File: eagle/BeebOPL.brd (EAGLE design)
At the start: 100 x 80 mm, 34 parts, among them IC1 LM324N, IC2 YM3014B, IC5 74LS02N, IC6 YM3812, IC7 74LS04N, IC9 74HCT688N, J1 1 MHz Bus, J2 Feed-through, J3 3.5mm Jack, J4 5V DC

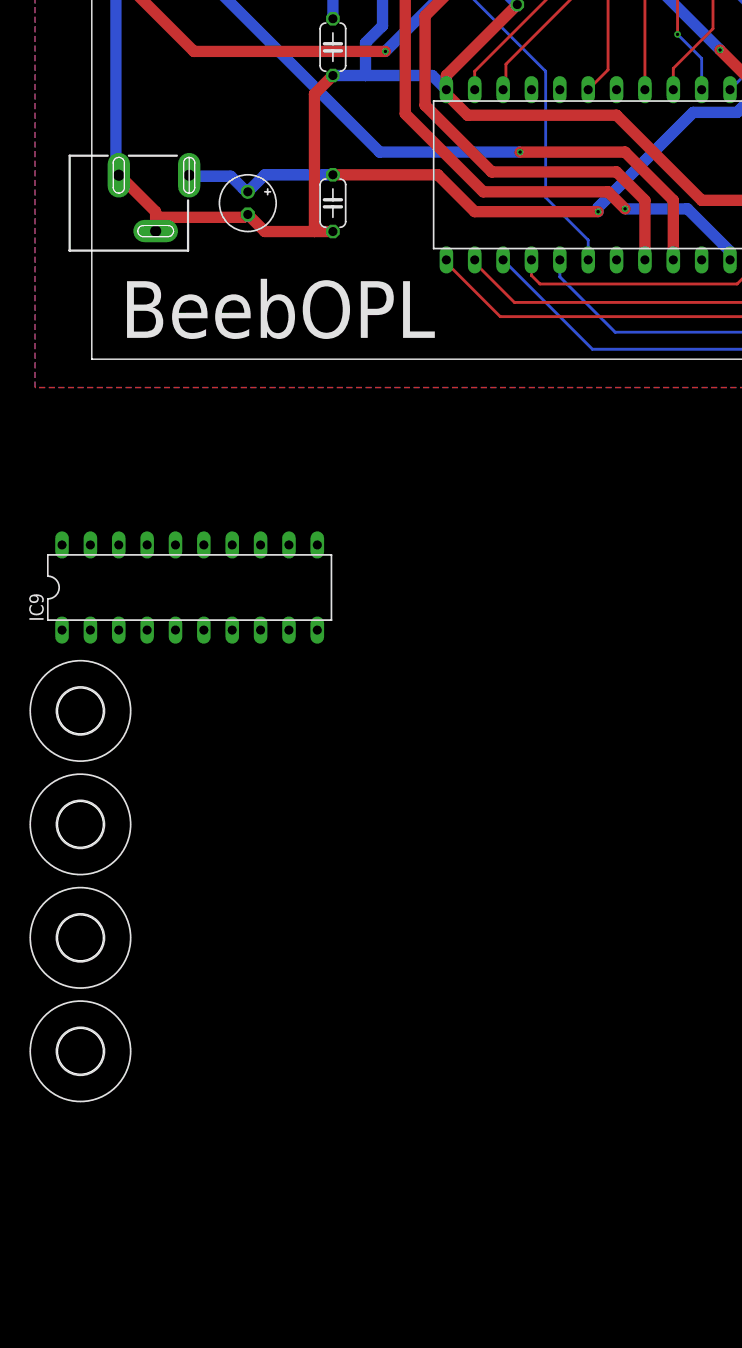
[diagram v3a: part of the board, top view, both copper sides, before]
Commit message: Added resistor networks
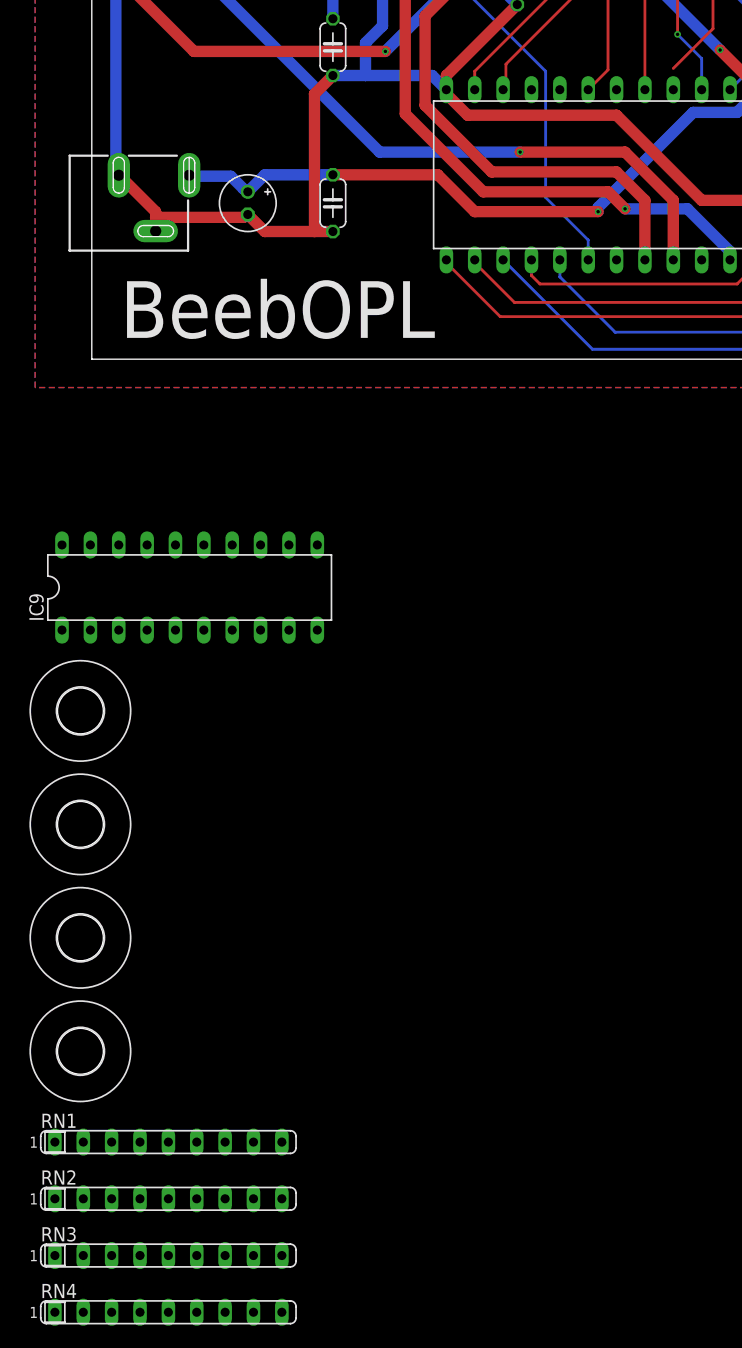
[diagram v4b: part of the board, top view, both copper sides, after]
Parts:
- added RN1, RN2, RN3, RN4: 2K2, resistor-sil:SIL9
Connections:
- net A0: now also RN3.2, RN4.2
- net A1: now also RN3.3, RN4.3
- net A2: now also RN3.4, RN4.4
- net A3: now also RN3.5, RN4.5
- net A4: now also RN3.6, RN4.6
- net A5: now also RN3.7, RN4.7
- net A6: now also RN3.8, RN4.8
- net A7: now also RN3.9, RN4.9
- net D0: now also RN1.2, RN2.2
- net D1: now also RN1.3, RN2.3
- net D2: now also RN1.4, RN2.4
- net D3: now also RN1.5, RN2.5
- net D4: now also RN1.6, RN2.6
- net D5: now also RN1.7, RN2.7
- net D6: now also RN1.8, RN2.8
- net D7: now also RN1.9, RN2.9
- net GND: now also RN2.1, RN4.1
- net VCC: now also RN1.1, RN3.1
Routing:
- net A0: track 77.6 -> 75.7 mm

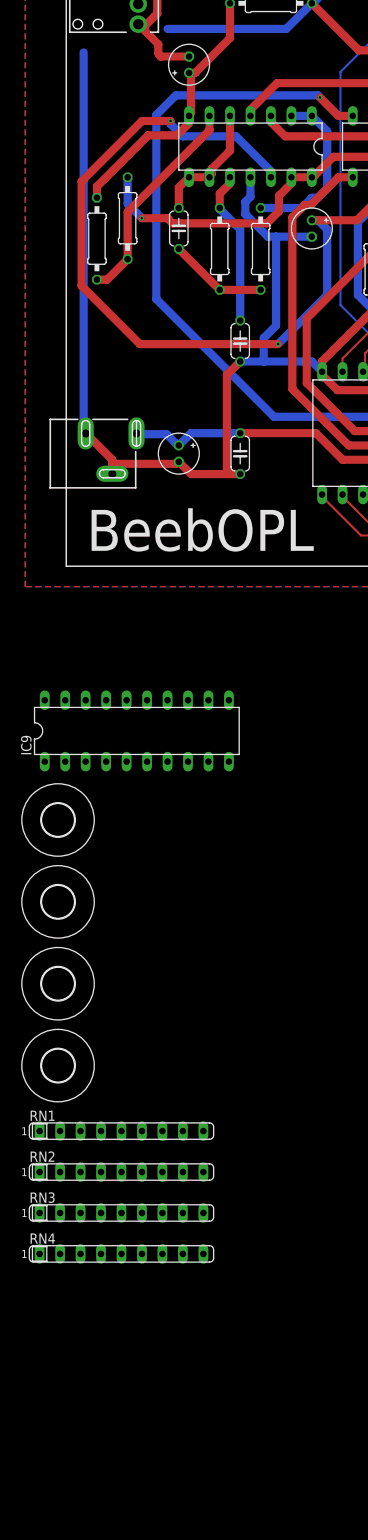
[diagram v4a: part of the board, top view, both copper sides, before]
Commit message: Added optional power regualtor
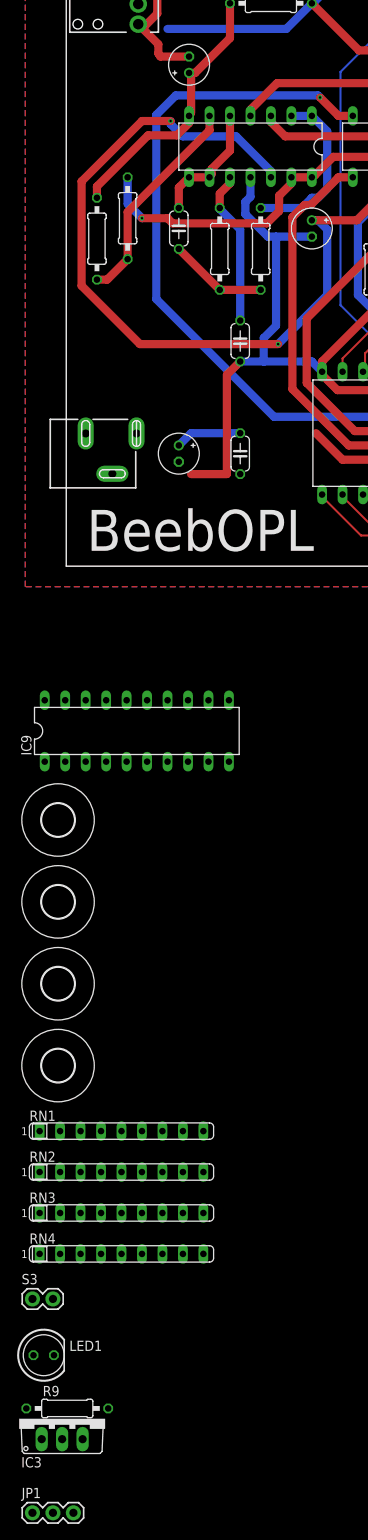
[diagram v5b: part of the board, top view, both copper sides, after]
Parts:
- added IC3: 7805TV, linear:TO220V
- added JP1: JUMPER-3PTH, SparkFun-Retired:1X03
- added LED1: (no value), led:LED5MM
- added R9: 470R, resistor:0207/10
- added S3: LED, SparkFun-Retired:1X02
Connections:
- new net N$25: LED1.A, R9.1, S3.2
- new net N$27: IC3.1, JP1.3
- new net N$28: C6.-, C7.2
- new net N$29: C6.+, C7.1
- net GND: now also IC3.2, LED1.K, S3.1; no longer C6.-, C7.2, J4.GND@1
- net VCC: now also IC3.3, JP1.1, JP1.2, R9.2; no longer C6.+, C7.1
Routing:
- net GND: track 408.9 -> 343.0 mm
- net VCC: track 186.5 -> 163.0 mm
- net N$29: track 0.00 -> 8.25 mm
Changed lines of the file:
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@@
 <attribute name="MF" value="" x="6.858" y="-85.344" size="1.778" layer="27" display="off"/>
 </element>
+<element name="S3" library="SparkFun-Retired" package="1X02" value="LED" x="-4.191" y="-90.932"/>
+<element name="LED1" library="led" package="LED5MM" value="" x="-2.794" y="-97.917"/>
+<element name="R9" library="resistor" package="0207/10" value="470R" x="0.127" y="-104.521"/>
+<element name="IC3" library="linear" package="TO220V" value="7805TV" x="-0.508" y="-105.791"/>
+<element name="JP1" library="SparkFun-Retired" package="1X03" value="JUMPER-3PTH" x="-4.191" y="-117.475"/>
 </elements>
 <signals>
@@
 <contactref element="C4" pad="2"/>
 <contactref element="IC5" pad="7"/>
-<contactref element="J4" pad="GND@1"/>
-<contactref element="J4" pad="GND@2"/>
-<contactref element="C6" pad="-"/>
-<contactref element="C7" pad="2"/>
 <contactref element="IC6" pad="GND"/>
 <contactref element="C8" pad="2"/>
@@
 <wire x1="74.1045" y1="20.6375" x2="64.389" y2="30.353" width="1.016" layer="1"/>
 <wire x1="15.494" y1="11.43" x2="19.939" y2="11.43" width="1.016" layer="1"/>
-<wire x1="19.939" y1="11.43" x2="21.59" y2="11.43" width="1.016" layer="1"/>
-<wire x1="13.97" y1="12.954" x2="15.494" y2="11.43" width="1.016" layer="1"/>
-<wire x1="5.715" y1="13.208" x2="5.715" y2="12.7" width="1.016" layer="1"/>
-<wire x1="5.715" y1="12.7" x2="5.715" y2="11.557" width="1.016" layer="1"/>
-<wire x1="2.54" y1="16.383" x2="5.715" y2="13.208" width="1.016" layer="1"/>
-<wire x1="5.715" y1="11.557" x2="5.72" y2="11.47" width="1.016" layer="1"/>
-<wire x1="2.54" y1="16.383" x2="2.42" y2="16.47" width="1.016" layer="1"/>
-<wire x1="5.715" y1="12.7" x2="13.589" y2="12.7" width="1.016" layer="1"/>
-<wire x1="13.589" y1="12.7" x2="13.97" y2="12.954" width="1.016" layer="1"/>
 <wire x1="22.86" y1="45.847" x2="22.86" y2="48.26" width="1.016" layer="16"/>
 <wire x1="22.225" y1="45.212" x2="22.86" y2="45.847" width="1.016" layer="16"/>
@@
 <wire x1="12.573" y1="66.675" x2="27.305" y2="66.675" width="1.016" layer="16"/>
 <wire x1="30.48" y1="69.85" x2="27.305" y2="66.675" width="1.016" layer="16"/>
-<wire x1="2.159" y1="63.754" x2="2.159" y2="17.399" width="1.016" layer="16"/>
-<wire x1="2.159" y1="17.399" x2="2.42" y2="17.138" width="1.016" layer="16"/>
-<wire x1="2.42" y1="17.138" x2="2.42" y2="16.47" width="1.016" layer="16"/>
 <polygon width="0.254" layer="16">
 <vertex x="-5.08" y="83.82"/>
@@
 <contactref element="RN2" pad="1"/>
 <contactref element="RN4" pad="1"/>
+<contactref element="LED1" pad="K"/>
+<contactref element="S3" pad="1"/>
+<contactref element="IC3" pad="2"/>
+<contactref element="J4" pad="GND@2"/>
+<wire x1="-1.524" y1="-97.917" x2="-0.508" y2="-108.331" width="0" layer="19" extent="1-1"/>
+<wire x1="-4.191" y1="-90.932" x2="-1.524" y2="-97.917" width="0" layer="19" extent="1-1"/>
+<wire x1="-3.302" y1="-85.344" x2="-4.191" y2="-90.932" width="0" layer="19" extent="1-1"/>
 <wire x1="-3.302" y1="-75.184" x2="-3.302" y2="-85.344" width="0" layer="19" extent="1-1"/>
 <wire x1="-2.667" y1="-24.257" x2="-3.302" y2="-75.184" width="0" layer="19" extent="1-1"/>
@@
 <wire x1="20.193" y1="-24.257" x2="17.653" y2="-24.257" width="0" layer="19" extent="1-1"/>
 <wire x1="19.939" y1="11.43" x2="17.653" y2="-16.637" width="0" layer="19" extent="1-1"/>
-<wire x1="3.937" y1="72.263" x2="2.159" y2="63.754" width="0" layer="19" extent="16-16"/>
-<wire x1="12.573" y1="66.675" x2="3.937" y2="72.263" width="0" layer="19" extent="16-16"/>
+<wire x1="5.72" y1="11.47" x2="15.494" y2="11.43" width="0" layer="19" extent="1-1"/>
+<wire x1="46.228" y1="58.674" x2="38.1" y2="48.26" width="0" layer="19" extent="1-1"/>
+<wire x1="3.937" y1="72.263" x2="12.573" y2="66.675" width="0" layer="19" extent="16-16"/>
 </signal>
 <signal name="D0">
@@
 <contactref element="IC1" pad="4"/>
 <contactref element="IC5" pad="14"/>
-<contactref element="J4" pad="PWR"/>
-<contactref element="C7" pad="1"/>
-<contactref element="C6" pad="+"/>
 <contactref element="IC6" pad="VSS"/>
 <contactref element="C8" pad="1"/>
@@
 <wire x1="43.18" y1="56.642" x2="39.878" y2="59.944" width="1.016" layer="16"/>
 <wire x1="43.18" y1="55.88" x2="43.18" y2="56.642" width="1.016" layer="16"/>
-<wire x1="15.494" y1="16.51" x2="21.59" y2="16.51" width="1.016" layer="16"/>
-<wire x1="13.97" y1="14.986" x2="15.494" y2="16.51" width="1.016" layer="16"/>
-<wire x1="12.446" y1="16.383" x2="8.763" y2="16.383" width="1.016" layer="16"/>
-<wire x1="13.589" y1="15.24" x2="12.446" y2="16.383" width="1.016" layer="16"/>
-<wire x1="8.763" y1="16.383" x2="8.72" y2="16.47" width="1.016" layer="16"/>
-<wire x1="13.589" y1="15.24" x2="13.97" y2="14.986" width="1.016" layer="16"/>
 <wire x1="59.69" y1="24.13" x2="64.77" y2="19.05" width="1.016" layer="16"/>
 <wire x1="82.677" y1="31.75" x2="81.28" y2="31.75" width="1.016" layer="16"/>
@@
 <wire x1="88.9" y1="13.97" x2="67.437" y2="13.97" width="1.016" layer="16"/>
 <wire x1="65.024" y1="18.669" x2="64.77" y2="19.05" width="1.016" layer="16"/>
-<wire x1="30.988" y1="16.51" x2="21.59" y2="16.51" width="1.016" layer="1"/>
 <wire x1="34.29" y1="13.208" x2="30.988" y2="16.51" width="1.016" layer="1"/>
 <wire x1="45.339" y1="13.208" x2="34.29" y2="13.208" width="1.016" layer="1"/>
@@
 <contactref element="RN1" pad="1"/>
 <contactref element="RN3" pad="1"/>
-<wire x1="93.98" y1="19.05" x2="82.677" y2="31.75" width="0" layer="19" extent="1-16"/>
-<wire x1="-2.667" y1="-16.637" x2="8.763" y2="16.383" width="0" layer="19" extent="16-16"/>
-<wire x1="12.573" y1="-24.257" x2="-2.667" y2="-16.637" width="0" layer="19" extent="1-1"/>
-<wire x1="-3.302" y1="-70.104" x2="12.573" y2="-24.257" width="0" layer="19" extent="1-1"/>
-<wire x1="-3.302" y1="-80.264" x2="-3.302" y2="-70.104" width="0" layer="19" extent="1-1"/>
+<contactref element="R9" pad="2"/>
+<contactref element="IC3" pad="3"/>
+<contactref element="JP1" pad="1"/>
+<contactref element="JP1" pad="2"/>
+<contactref element="J4" pad="PWR"/>
+<wire x1="-1.651" y1="-117.475" x2="-4.191" y2="-117.475" width="0" layer="19" extent="1-1"/>
+<wire x1="2.032" y1="-108.331" x2="-1.651" y2="-117.475" width="0" layer="19" extent="1-1"/>
+<wire x1="5.207" y1="-104.521" x2="2.032" y2="-108.331" width="0" layer="19" extent="1-1"/>
+<wire x1="-3.302" y1="-80.264" x2="5.207" y2="-104.521" width="0" layer="19" extent="1-1"/>
+<wire x1="-3.302" y1="-70.104" x2="-3.302" y2="-80.264" width="0" layer="19" extent="1-1"/>
+<wire x1="12.573" y1="-24.257" x2="-3.302" y2="-70.104" width="0" layer="19" extent="1-1"/>
+<wire x1="-2.667" y1="-16.637" x2="12.573" y2="-24.257" width="0" layer="19" extent="1-1"/>
+<wire x1="8.72" y1="16.47" x2="-2.667" y2="-16.637" width="0" layer="19" extent="1-1"/>
+<wire x1="30.988" y1="16.51" x2="8.72" y2="16.47" width="0" layer="19" extent="1-1"/>
+<wire x1="82.677" y1="31.75" x2="93.98" y2="19.05" width="0" layer="19" extent="1-16"/>
 </signal>
 <signal name="N$4">
@@
 <wire x1="-0.127" y1="-16.637" x2="44.45" y2="24.13" width="0" layer="19" extent="1-1"/>
 </signal>
+<signal name="N$25">
+<contactref element="LED1" pad="A"/>
+<contactref element="R9" pad="1"/>
+<contactref element="S3" pad="2"/>
+<wire x1="-4.064" y1="-97.917" x2="-4.953" y2="-104.521" width="0" layer="19" extent="1-1"/>
+<wire x1="-1.651" y1="-90.932" x2="-4.064" y2="-97.917" width="0" layer="19" extent="1-1"/>
+</signal>
+<signal name="N$27">
+<contactref element="JP1" pad="3"/>
+<contactref element="IC3" pad="1"/>
+<wire x1="-3.048" y1="-108.331" x2="0.889" y2="-117.475" width="0" layer="19" extent="1-1"/>
+</signal>
+<signal name="N$29" class="1">
+<contactref element="C7" pad="1"/>
+<contactref element="C6" pad="+"/>
+<wire x1="15.494" y1="16.51" x2="21.59" y2="16.51" width="1.016" layer="16"/>
+<wire x1="13.97" y1="14.986" x2="15.494" y2="16.51" width="1.016" layer="16"/>
+</signal>
+<signal name="N$28" class="3">
+<contactref element="C6" pad="-"/>
+<contactref element="C7" pad="2"/>
+<wire x1="13.97" y1="12.954" x2="21.59" y2="11.43" width="0" layer="19" extent="1-1"/>
+</signal>
 </signals>

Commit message: Added power options
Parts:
- removed S3: LED, SparkFun-Retired:1X02
- added JP2, JP3, JP4: (no value), pinhead:1X02/90
- added U$1: IRFD9024DIL, YMSynth:FET-DIL
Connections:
- removed net N$28: C6.-, C7.2
- removed net N$29: C6.+, C7.1
- net GND: now also C6.-, C7.2, JP2.2, JP3.2, JP4.2, U$1.G; no longer S3.1
- net N$17: now also JP3.1
- net N$25: now also JP4.1; no longer S3.2
- net VCC: now also C6.+, C7.1, JP2.1, U$1.D, U$1.D1, U$1.S
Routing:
- net VCC: track 163.0 -> 171.2 mm
- net N$29: track 8.25 -> 0.00 mm
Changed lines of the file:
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@@
 <attribute name="MF" value="" x="6.858" y="-85.344" size="1.778" layer="27" display="off"/>
 </element>
-<element name="S3" library="SparkFun-Retired" package="1X02" value="LED" x="-4.191" y="-90.932"/>
 <element name="LED1" library="led" package="LED5MM" value="" x="-2.794" y="-97.917"/>
 <element name="R9" library="resistor" package="0207/10" value="470R" x="0.127" y="-104.521"/>
 <element name="IC3" library="linear" package="TO220V" value="7805TV" x="-0.508" y="-105.791"/>
 <element name="JP1" library="SparkFun-Retired" package="1X03" value="JUMPER-3PTH" x="-4.191" y="-117.475"/>
+<element name="U$1" library="YMSynth" package="FET-DIL" value="IRFD9024DIL" x="-0.127" y="-125.984"/>
+<element name="JP2" library="pinhead" package="1X02/90" value="" x="-11.049" y="-124.841"/>
+<element name="JP3" library="pinhead" package="1X02/90" value="" x="-20.955" y="-124.841"/>
+<element name="JP4" library="pinhead" package="1X02/90" value="" x="-30.861" y="-124.841"/>
 </elements>
 <signals>
@@
 <contactref element="RN4" pad="1"/>
 <contactref element="LED1" pad="K"/>
-<contactref element="S3" pad="1"/>
 <contactref element="IC3" pad="2"/>
 <contactref element="J4" pad="GND@2"/>
+<contactref element="U$1" pad="G"/>
+<contactref element="JP2" pad="2"/>
+<contactref element="C6" pad="-"/>
+<contactref element="C7" pad="2"/>
+<contactref element="JP3" pad="2"/>
+<contactref element="JP4" pad="2"/>
+<wire x1="-19.685" y1="-128.651" x2="-29.591" y2="-128.651" width="0" layer="19" extent="1-1"/>
+<wire x1="-9.779" y1="-128.651" x2="-19.685" y2="-128.651" width="0" layer="19" extent="1-1"/>
+<wire x1="3.683" y1="-127.254" x2="-9.779" y2="-128.651" width="0" layer="19" extent="1-1"/>
+<wire x1="-0.508" y1="-108.331" x2="3.683" y2="-127.254" width="0" layer="19" extent="1-1"/>
 <wire x1="-1.524" y1="-97.917" x2="-0.508" y2="-108.331" width="0" layer="19" extent="1-1"/>
-<wire x1="-4.191" y1="-90.932" x2="-1.524" y2="-97.917" width="0" layer="19" extent="1-1"/>
-<wire x1="-3.302" y1="-85.344" x2="-4.191" y2="-90.932" width="0" layer="19" extent="1-1"/>
+<wire x1="-3.302" y1="-85.344" x2="-1.524" y2="-97.917" width="0" layer="19" extent="1-1"/>
 <wire x1="-3.302" y1="-75.184" x2="-3.302" y2="-85.344" width="0" layer="19" extent="1-1"/>
 <wire x1="-2.667" y1="-24.257" x2="-3.302" y2="-75.184" width="0" layer="19" extent="1-1"/>
@@
 <wire x1="20.193" y1="-24.257" x2="17.653" y2="-24.257" width="0" layer="19" extent="1-1"/>
 <wire x1="19.939" y1="11.43" x2="17.653" y2="-16.637" width="0" layer="19" extent="1-1"/>
-<wire x1="5.72" y1="11.47" x2="15.494" y2="11.43" width="0" layer="19" extent="1-1"/>
+<wire x1="21.59" y1="11.43" x2="19.939" y2="11.43" width="0" layer="19" extent="1-1"/>
+<wire x1="13.97" y1="12.954" x2="15.494" y2="11.43" width="0" layer="19" extent="1-1"/>
+<wire x1="5.72" y1="11.47" x2="13.97" y2="12.954" width="0" layer="19" extent="1-1"/>
 <wire x1="46.228" y1="58.674" x2="38.1" y2="48.26" width="0" layer="19" extent="1-1"/>
 <wire x1="3.937" y1="72.263" x2="12.573" y2="66.675" width="0" layer="19" extent="16-16"/>
@@
 <contactref element="JP1" pad="1"/>
 <contactref element="JP1" pad="2"/>
+<contactref element="U$1" pad="S"/>
 <contactref element="J4" pad="PWR"/>
+<contactref element="U$1" pad="D1"/>
+<contactref element="U$1" pad="D"/>
+<contactref element="JP2" pad="1"/>
+<contactref element="C7" pad="1"/>
+<contactref element="C6" pad="+"/>
+<wire x1="15.494" y1="16.51" x2="21.59" y2="16.51" width="1.016" layer="16"/>
+<wire x1="13.97" y1="14.986" x2="15.494" y2="16.51" width="1.016" layer="16"/>
+<wire x1="-3.937" y1="-127.254" x2="-12.319" y2="-128.651" width="0" layer="19" extent="1-1"/>
 <wire x1="-1.651" y1="-117.475" x2="-4.191" y2="-117.475" width="0" layer="19" extent="1-1"/>
+<wire x1="3.683" y1="-124.714" x2="-3.937" y2="-124.714" width="0" layer="19" extent="1-1"/>
 <wire x1="2.032" y1="-108.331" x2="-1.651" y2="-117.475" width="0" layer="19" extent="1-1"/>
 <wire x1="5.207" y1="-104.521" x2="2.032" y2="-108.331" width="0" layer="19" extent="1-1"/>
@@
 <wire x1="-2.667" y1="-16.637" x2="12.573" y2="-24.257" width="0" layer="19" extent="1-1"/>
 <wire x1="8.72" y1="16.47" x2="-2.667" y2="-16.637" width="0" layer="19" extent="1-1"/>
-<wire x1="30.988" y1="16.51" x2="8.72" y2="16.47" width="0" layer="19" extent="1-1"/>
+<wire x1="13.97" y1="14.986" x2="8.72" y2="16.47" width="0" layer="19" extent="1-1"/>
+<wire x1="30.988" y1="16.51" x2="21.59" y2="16.51" width="0" layer="19" extent="1-1"/>
 <wire x1="82.677" y1="31.75" x2="93.98" y2="19.05" width="0" layer="19" extent="1-16"/>
+<wire x1="-4.191" y1="-117.475" x2="-3.937" y2="-124.714" width="0" layer="19" extent="1-1"/>
+<wire x1="-3.937" y1="-124.714" x2="-3.937" y2="-127.254" width="0" layer="19" extent="1-1"/>
 </signal>
 <signal name="N$4">
@@
 <wire x1="11.303" y1="76.2" x2="11.303" y2="68.58" width="1.016" layer="1"/>
 <wire x1="9.779" y1="67.056" x2="8.937" y2="67.263" width="1.016" layer="1"/>
+<contactref element="JP3" pad="1"/>
+<wire x1="11.684" y1="63.246" x2="-22.225" y2="-128.651" width="0" layer="19" extent="1-1"/>
 </signal>
 <signal name="N$18" class="2">
@@
 <contactref element="LED1" pad="A"/>
 <contactref element="R9" pad="1"/>
-<contactref element="S3" pad="2"/>
+<contactref element="JP4" pad="1"/>
+<wire x1="-4.953" y1="-104.521" x2="-32.131" y2="-128.651" width="0" layer="19" extent="1-1"/>
 <wire x1="-4.064" y1="-97.917" x2="-4.953" y2="-104.521" width="0" layer="19" extent="1-1"/>
-<wire x1="-1.651" y1="-90.932" x2="-4.064" y2="-97.917" width="0" layer="19" extent="1-1"/>
 </signal>
 <signal name="N$27">
@@
 <wire x1="-3.048" y1="-108.331" x2="0.889" y2="-117.475" width="0" layer="19" extent="1-1"/>
 </signal>
-<signal name="N$29" class="1">
-<contactref element="C7" pad="1"/>
-<contactref element="C6" pad="+"/>
-<wire x1="15.494" y1="16.51" x2="21.59" y2="16.51" width="1.016" layer="16"/>
-<wire x1="13.97" y1="14.986" x2="15.494" y2="16.51" width="1.016" layer="16"/>
-</signal>
-<signal name="N$28" class="3">
-<contactref element="C6" pad="-"/>
-<contactref element="C7" pad="2"/>
-<wire x1="13.97" y1="12.954" x2="21.59" y2="11.43" width="0" layer="19" extent="1-1"/>
-</signal>
 </signals>
